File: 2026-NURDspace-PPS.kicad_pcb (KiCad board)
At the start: 4 copper layers, 90 x 85 mm, 122 parts, among them J101 UJ20-C-H-C-4-SMT-TR, Q101 BSN20, Q102 BSN20, Q103 BSN20, Q104 BSN20, Q105 XTR_NFET_SI4134, Q106 XTR_NFET_SI4134, SW101 430172085816, U101 1G126, U102 1G126, U103 1G126, U104 1G126, U105 1G126, U106 1G126, U107 74HC595, U108 1G126, U109 1G126, U110 3.3V, U111 AP33772S, U112 74HC595, U113 1G126, U114 1G126, U115 1G126, U116 1G126, U117 74HC595, U118 1G126, U119 1G126, U120 74HC595, U121 1G126, U122 1G126, U123 481RV12172100, U124 ESP32-S3-WROOM-1

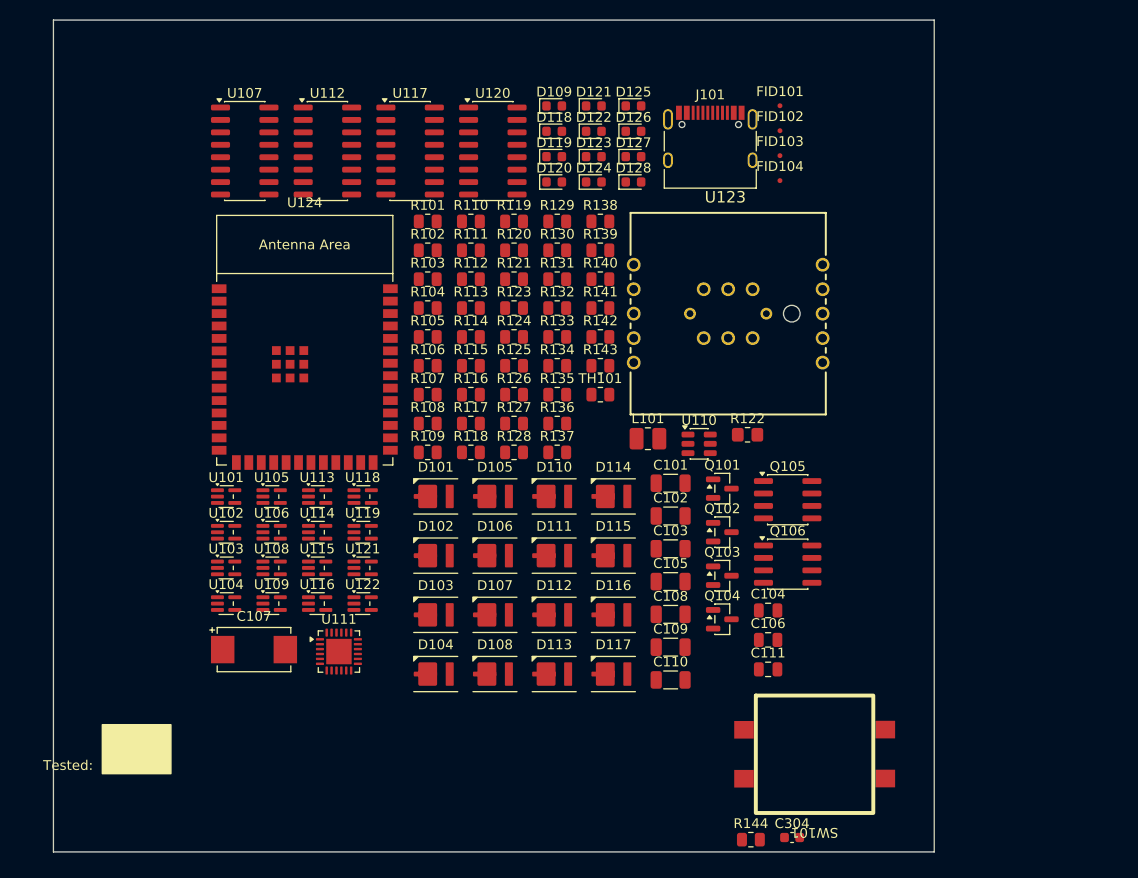
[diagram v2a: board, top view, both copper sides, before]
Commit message: Drawn the schematic
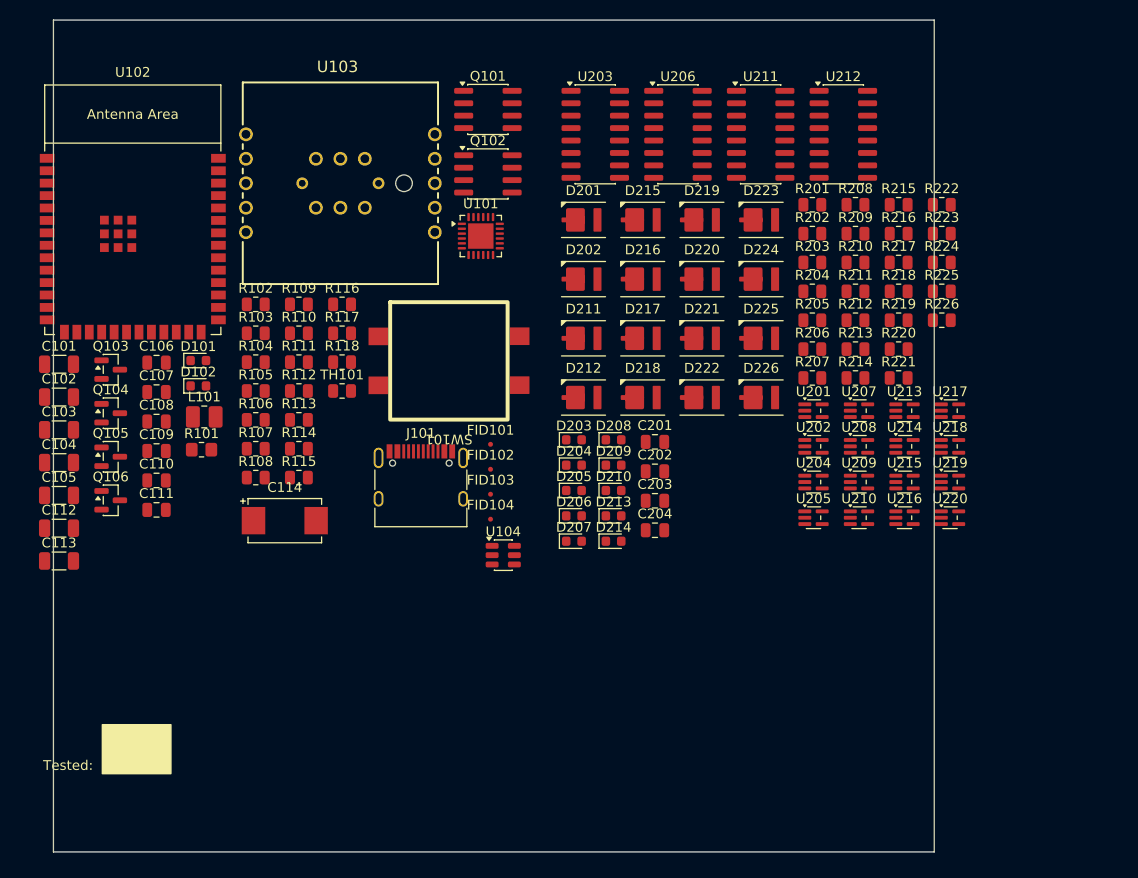
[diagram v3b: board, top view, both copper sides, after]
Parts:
- removed C304: 100nF, Capacitor_SMD:C_0603_1608Metric
- removed D103, D104, D105, D106, D107, D108, D110, D111, D112, D113, D114, D115, D116, D117: MXA8-PW40-0000, 0_NRD_footprints:LED_Luxeon3535_3.5x3.7mm
- removed D109: amber, LED_SMD:LED_0603_1608Metric
- removed D118: brightgreen, LED_SMD:LED_0603_1608Metric
- removed D119, D120, D121, D122, D123, D124, D125, D126, D127, D128: Led_0603_superred_generic, LED_SMD:LED_0603_1608Metric
- removed R119, R120, R123, R124, R125, R126: 39R, Resistor_SMD:R_0805_2012Metric
- removed R121, R127, R128, R130, R131, R137, R138, R144: 5K1, Resistor_SMD:R_0805_2012Metric
- removed R122: 5mR, Resistor_SMD:R_0805_2012Metric_Pad1.20x1.40mm_HandSolder
- removed R129: 180R, Resistor_SMD:R_0805_2012Metric
- removed R132, R133, R134, R135, R136, R139, R140, R141, R142, R143: 270R, Resistor_SMD:R_0805_2012Metric
- removed U105, U106, U108, U109, U113, U114, U115, U116, U118, U119, U121, U122: 1G126, Package_TO_SOT_SMD:SOT-353_SC-70-5
- removed U107, U112, U117, U120: 74HC595, Package_SO:SOIC-16_3.9x9.9mm_P1.27mm
- removed U110: 3.3V, Package_TO_SOT_SMD:TSOT-23-6
- removed U111: AP33772S, Package_DFN_QFN:QFN-24-1EP_4x4mm_P0.5mm_EP2.6x2.6mm
- removed U123: 481RV12172100, 0_NRD_footprints:481RV12172100
- removed U124: ESP32-S3-WROOM-1, 0_NRD_footprints:ESP32-S3-WROOM-1
- added C112: 6.8uF, Capacitor_SMD:C_1206_3216Metric, F.Cu at (103.1, 66.9)
- added C113: 1uF, Capacitor_SMD:C_1206_3216Metric, F.Cu at (103.1, 70.3)
- added C114: 180uF, 0_NRD_footprints:CP_Wurth_WCAP-PHLE-L7.3W4.3H1.9, F.Cu at (126.1, 66.2)
- added C201: 100nF, Capacitor_SMD:C_0805_2012Metric, F.Cu at (164.0, 58.1)
- added C202: 100nF, Capacitor_SMD:C_0805_2012Metric, F.Cu at (164.0, 61.1)
- added C203: 100nF, Capacitor_SMD:C_0805_2012Metric, F.Cu at (164.0, 64.1)
- added C204: 100nF, Capacitor_SMD:C_0805_2012Metric, F.Cu at (164.0, 67.1)
- added D201: MXA8-PW40-0000, 0_NRD_footprints:LED_Luxeon3535_3.5x3.7mm, F.Cu at (156.7, 35.4)
- added D202: MXA8-PW40-0000, 0_NRD_footprints:LED_Luxeon3535_3.5x3.7mm, F.Cu at (156.7, 41.5)
- added D203: Led_0603_superred_generic, LED_SMD:LED_0603_1608Metric, F.Cu at (155.7, 57.9)
- added D204: Led_0603_superred_generic, LED_SMD:LED_0603_1608Metric, F.Cu at (155.7, 60.5)
- added D205: Led_0603_superred_generic, LED_SMD:LED_0603_1608Metric, F.Cu at (155.7, 63.1)
- added D206: Led_0603_superred_generic, LED_SMD:LED_0603_1608Metric, F.Cu at (155.7, 65.7)
- added D207: Led_0603_superred_generic, LED_SMD:LED_0603_1608Metric, F.Cu at (155.7, 68.2)
- added D208: Led_0603_superred_generic, LED_SMD:LED_0603_1608Metric, F.Cu at (159.7, 57.9)
- added D209: Led_0603_superred_generic, LED_SMD:LED_0603_1608Metric, F.Cu at (159.7, 60.5)
- added D210: Led_0603_superred_generic, LED_SMD:LED_0603_1608Metric, F.Cu at (159.7, 63.1)
- added D211: MXA8-PW40-0000, 0_NRD_footprints:LED_Luxeon3535_3.5x3.7mm, F.Cu at (156.7, 47.5)
- added D212: MXA8-PW40-0000, 0_NRD_footprints:LED_Luxeon3535_3.5x3.7mm, F.Cu at (156.7, 53.6)
- added D213: Led_0603_superred_generic, LED_SMD:LED_0603_1608Metric, F.Cu at (159.7, 65.7)
- added D214: Led_0603_superred_generic, LED_SMD:LED_0603_1608Metric, F.Cu at (159.7, 68.2)
- added D215: MXA8-PW40-0000, 0_NRD_footprints:LED_Luxeon3535_3.5x3.7mm, F.Cu at (162.7, 35.4)
- added D216: MXA8-PW40-0000, 0_NRD_footprints:LED_Luxeon3535_3.5x3.7mm, F.Cu at (162.7, 41.5)
- added D217: MXA8-PW40-0000, 0_NRD_footprints:LED_Luxeon3535_3.5x3.7mm, F.Cu at (162.7, 47.5)
- added D218: MXA8-PW40-0000, 0_NRD_footprints:LED_Luxeon3535_3.5x3.7mm, F.Cu at (162.7, 53.6)
- added D219: MXA8-PW40-0000, 0_NRD_footprints:LED_Luxeon3535_3.5x3.7mm, F.Cu at (168.8, 35.4)
- added D220: MXA8-PW40-0000, 0_NRD_footprints:LED_Luxeon3535_3.5x3.7mm, F.Cu at (168.8, 41.5)
- added D221: MXA8-PW40-0000, 0_NRD_footprints:LED_Luxeon3535_3.5x3.7mm, F.Cu at (168.8, 47.5)
- added D222: MXA8-PW40-0000, 0_NRD_footprints:LED_Luxeon3535_3.5x3.7mm, F.Cu at (168.8, 53.6)
- added D223: MXA8-PW40-0000, 0_NRD_footprints:LED_Luxeon3535_3.5x3.7mm, F.Cu at (174.8, 35.4)
- added D224: MXA8-PW40-0000, 0_NRD_footprints:LED_Luxeon3535_3.5x3.7mm, F.Cu at (174.8, 41.5)
- added D225: MXA8-PW40-0000, 0_NRD_footprints:LED_Luxeon3535_3.5x3.7mm, F.Cu at (174.8, 47.5)
- added D226: MXA8-PW40-0000, 0_NRD_footprints:LED_Luxeon3535_3.5x3.7mm, F.Cu at (174.8, 53.6)
- added R201: 39R, Resistor_SMD:R_0805_2012Metric, F.Cu at (180.0, 33.9)
- added R202: 39R, Resistor_SMD:R_0805_2012Metric, F.Cu at (180.0, 36.8)
- added R203: 270R, Resistor_SMD:R_0805_2012Metric, F.Cu at (180.0, 39.8)
- added R204: 270R, Resistor_SMD:R_0805_2012Metric, F.Cu at (180.0, 42.7)
- added R205: 270R, Resistor_SMD:R_0805_2012Metric, F.Cu at (180.0, 45.7)
- added R206: 270R, Resistor_SMD:R_0805_2012Metric, F.Cu at (180.0, 48.6)
- added R207: 270R, Resistor_SMD:R_0805_2012Metric, F.Cu at (180.0, 51.6)
- added R208: 270R, Resistor_SMD:R_0805_2012Metric, F.Cu at (184.5, 33.9)
- added R209: 270R, Resistor_SMD:R_0805_2012Metric, F.Cu at (184.5, 36.8)
- added R210: 270R, Resistor_SMD:R_0805_2012Metric, F.Cu at (184.5, 39.8)
- added R211: 39R, Resistor_SMD:R_0805_2012Metric, F.Cu at (184.5, 42.7)
- added R212: 39R, Resistor_SMD:R_0805_2012Metric, F.Cu at (184.5, 45.7)
- added R213: 270R, Resistor_SMD:R_0805_2012Metric, F.Cu at (184.5, 48.6)
- added R214: 270R, Resistor_SMD:R_0805_2012Metric, F.Cu at (184.5, 51.6)
- added R215: 39R, Resistor_SMD:R_0805_2012Metric, F.Cu at (188.9, 33.9)
- added R216: 39R, Resistor_SMD:R_0805_2012Metric, F.Cu at (188.9, 36.8)
- added R217: 39R, Resistor_SMD:R_0805_2012Metric, F.Cu at (188.9, 39.8)
- added R218: 39R, Resistor_SMD:R_0805_2012Metric, F.Cu at (188.9, 42.7)
- added R219: 39R, Resistor_SMD:R_0805_2012Metric, F.Cu at (188.9, 45.7)
- added R220: 39R, Resistor_SMD:R_0805_2012Metric, F.Cu at (188.9, 48.6)
- added R221: 39R, Resistor_SMD:R_0805_2012Metric, F.Cu at (188.9, 51.6)
- added R222: 39R, Resistor_SMD:R_0805_2012Metric, F.Cu at (193.3, 33.9)
- added R223: 39R, Resistor_SMD:R_0805_2012Metric, F.Cu at (193.3, 36.8)
- added R224: 39R, Resistor_SMD:R_0805_2012Metric, F.Cu at (193.3, 39.8)
- added R225: 39R, Resistor_SMD:R_0805_2012Metric, F.Cu at (193.3, 42.7)
- added R226: 39R, Resistor_SMD:R_0805_2012Metric, F.Cu at (193.3, 45.7)
- added U201: 1G126, Package_TO_SOT_SMD:SOT-353_SC-70-5, F.Cu at (180.2, 54.9)
- added U202: 1G126, Package_TO_SOT_SMD:SOT-353_SC-70-5, F.Cu at (180.2, 58.6)
- added U203: 74HC595, Package_SO:SOIC-16_3.9x9.9mm_P1.27mm, F.Cu at (157.9, 26.7)
- added U204: 1G126, Package_TO_SOT_SMD:SOT-353_SC-70-5, F.Cu at (180.2, 62.2)
- added U205: 1G126, Package_TO_SOT_SMD:SOT-353_SC-70-5, F.Cu at (180.2, 65.8)
- added U206: 74HC595, Package_SO:SOIC-16_3.9x9.9mm_P1.27mm, F.Cu at (166.3, 26.7)
- added U207: 1G126, Package_TO_SOT_SMD:SOT-353_SC-70-5, F.Cu at (184.8, 54.9)
- added U208: 1G126, Package_TO_SOT_SMD:SOT-353_SC-70-5, F.Cu at (184.8, 58.6)
- added U209: 1G126, Package_TO_SOT_SMD:SOT-353_SC-70-5, F.Cu at (184.8, 62.2)
- added U210: 1G126, Package_TO_SOT_SMD:SOT-353_SC-70-5, F.Cu at (184.8, 65.8)
- added U211: 74HC595, Package_SO:SOIC-16_3.9x9.9mm_P1.27mm, F.Cu at (174.8, 26.7)
- added U212: 74HC595, Package_SO:SOIC-16_3.9x9.9mm_P1.27mm, F.Cu at (183.2, 26.7)
- added U213: 1G126, Package_TO_SOT_SMD:SOT-353_SC-70-5, F.Cu at (189.5, 54.9)
- added U214: 1G126, Package_TO_SOT_SMD:SOT-353_SC-70-5, F.Cu at (189.5, 58.6)
- added U215: 1G126, Package_TO_SOT_SMD:SOT-353_SC-70-5, F.Cu at (189.5, 62.2)
- added U216: 1G126, Package_TO_SOT_SMD:SOT-353_SC-70-5, F.Cu at (189.5, 65.8)
- added U217: 1G126, Package_TO_SOT_SMD:SOT-353_SC-70-5, F.Cu at (194.1, 54.9)
- added U218: 1G126, Package_TO_SOT_SMD:SOT-353_SC-70-5, F.Cu at (194.1, 58.6)
- added U219: 1G126, Package_TO_SOT_SMD:SOT-353_SC-70-5, F.Cu at (194.1, 62.2)
- added U220: 1G126, Package_TO_SOT_SMD:SOT-353_SC-70-5, F.Cu at (194.1, 65.8)
- C104: value 100nF -> 6.8uF; footprint Capacitor_SMD:C_0805_2012Metric -> Capacitor_SMD:C_1206_3216Metric
- C107: value 180uF -> 100nF; footprint 0_NRD_footprints:CP_Wurth_WCAP-PHLE-L7.3W4.3H1.9 -> Capacitor_SMD:C_0805_2012Metric
- C108, C110: value 6.8uF -> 100nF; footprint Capacitor_SMD:C_1206_3216Metric -> Capacitor_SMD:C_0805_2012Metric
- C109: value 1uF -> 100nF; footprint Capacitor_SMD:C_1206_3216Metric -> Capacitor_SMD:C_0805_2012Metric
- D101: value MXA8-PW40-0000 -> brightgreen; footprint 0_NRD_footprints:LED_Luxeon3535_3.5x3.7mm -> LED_SMD:LED_0603_1608Metric
- D102: value MXA8-PW40-0000 -> amber; footprint 0_NRD_footprints:LED_Luxeon3535_3.5x3.7mm -> LED_SMD:LED_0603_1608Metric
- Q101, Q102: value BSN20 -> XTR_NFET_SI4134; footprint Package_TO_SOT_SMD:SOT-23 -> Package_SO:SOIC-8_3.9x4.9mm_P1.27mm
- Q105, Q106: value XTR_NFET_SI4134 -> BSN20; footprint Package_SO:SOIC-8_3.9x4.9mm_P1.27mm -> Package_TO_SOT_SMD:SOT-23
- R101: value 5K1 -> 5mR; footprint Resistor_SMD:R_0805_2012Metric -> Resistor_SMD:R_0805_2012Metric_Pad1.20x1.40mm_HandSolder
- R105: value 39R -> 180R
- R106, R107, R108, R109, R110, R111, R112, R117, R118: value 39R -> 5K1
- U101: value 1G126 -> AP33772S; footprint Package_TO_SOT_SMD:SOT-353_SC-70-5 -> Package_DFN_QFN:QFN-24-1EP_4x4mm_P0.5mm_EP2.6x2.6mm
- U102: value 1G126 -> ESP32-S3-WROOM-1; footprint Package_TO_SOT_SMD:SOT-353_SC-70-5 -> 0_NRD_footprints:ESP32-S3-WROOM-1
- U103: value 1G126 -> 481RV12172100; footprint Package_TO_SOT_SMD:SOT-353_SC-70-5 -> 0_NRD_footprints:481RV12172100
- U104: value 1G126 -> 3.3V; footprint Package_TO_SOT_SMD:SOT-353_SC-70-5 -> Package_TO_SOT_SMD:TSOT-23-6
- moved C104 74.0 mm to (103.1, 60.2)
- moved Q106 69.5 mm to (108.4, 64.1)
- moved Q105 69.3 mm to (108.4, 59.6)
- moved C106 68.6 mm to (113.0, 50.0)
- moved Q103 65.9 mm to (108.4, 50.7)
- moved Q104 65.9 mm to (108.4, 55.2)
- moved C111 64.6 mm to (113.0, 65.0)
- moved C101 63.7 mm to (103.1, 50.2)
- moved C102 63.7 mm to (103.1, 53.5)
- moved C103 63.7 mm to (103.1, 56.9)
- moved C105 63.1 mm to (103.1, 63.6)
- moved C110 56.3 mm to (113.0, 62.0)
- moved C109 56.2 mm to (113.0, 59.0)
- moved C108 56.1 mm to (113.0, 56.0)
- moved SW101 54.9 mm to (142.9, 49.8)
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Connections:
- C101 pad 1: unconnected-(C101-Pad1) -> Net-(U101-VCC)
- C101 pad 2: unconnected-(C101-Pad2) -> GND
- C102 pad 1: unconnected-(C102-Pad1) -> Net-(U101-VCC)
- C102 pad 2: unconnected-(C102-Pad2) -> GND
- C103 pad 1: unconnected-(C103-Pad1) -> VBUS
- C103 pad 2: unconnected-(C103-Pad2) -> GND
- C104 pad 1: unconnected-(C104-Pad1) -> VBUS
- C104 pad 2: unconnected-(C104-Pad2) -> GND
- C105 pad 1: unconnected-(C105-Pad1) -> +5V
- C105 pad 2: unconnected-(C105-Pad2) -> GND
- C106 pad 1: unconnected-(C106-Pad1) -> Net-(U101-V18)
- C106 pad 2: unconnected-(C106-Pad2) -> GND
- C107 pad 1: unconnected-(C107-Pad1) -> ESP_BOOTSEL
- C107 pad 2: unconnected-(C107-Pad2) -> GND
- C108 pad 1: unconnected-(C108-Pad1) -> +3.3V
- C108 pad 2: unconnected-(C108-Pad2) -> GND
- C109 pad 1: unconnected-(C109-Pad1) -> Net-(U101-IFB)
- C109 pad 2: unconnected-(C109-Pad2) -> GND
- C110 pad 1: unconnected-(C110-Pad1) -> Net-(U102-EN)
- C110 pad 2: unconnected-(C110-Pad2) -> GND
- C111 pad 1: unconnected-(C111-Pad1) -> Net-(U104-BST)
- C111 pad 2: unconnected-(C111-Pad2) -> Net-(U104-SW)
- D101 pad 1: unconnected-(D101-K-Pad1) -> GND
- D101 pad 2: unconnected-(D101-A-Pad2) -> Net-(D101-A)
- D102 pad 1: unconnected-(D102-K-Pad1) -> GND
- D102 pad 2: unconnected-(D102-A-Pad2) -> Net-(D102-A)
- J101 pad A1: Net-(J101-GND-PadA1) -> GND
- J101 pad A12: Net-(J101-GND-PadA1) -> GND
- J101 pad A4: Net-(J101-VBUS-PadA4) -> Net-(U101-ISENP)
- J101 pad A5: unconnected-(J101-CC1-PadA5) -> Net-(J101-CC1)
- J101 pad A6: unconnected-(J101-D+-PadA6) -> D+
- J101 pad A7: unconnected-(J101-D--PadA7) -> D-
- J101 pad A9: Net-(J101-VBUS-PadA4) -> Net-(U101-ISENP)
- J101 pad B1: Net-(J101-GND-PadA1) -> GND
- J101 pad B12: Net-(J101-GND-PadA1) -> GND
- J101 pad B4: Net-(J101-VBUS-PadA4) -> Net-(U101-ISENP)
- J101 pad B5: unconnected-(J101-CC2-PadB5) -> Net-(J101-CC2)
- J101 pad B6: unconnected-(J101-D+-PadB6) -> D+
- J101 pad B7: unconnected-(J101-D--PadB7) -> D-
- J101 pad B9: Net-(J101-VBUS-PadA4) -> Net-(U101-ISENP)
- J101 pad S1: unconnected-(J101-SHIELD-PadS1) -> GND
- L101 pad 1: unconnected-(L101-Pad1) -> Net-(U104-SW)
- L101 pad 2: unconnected-(L101-Pad2) -> +3.3V
- Q101 pad 1: unconnected-(Q101-G-Pad1) -> Net-(Q101-S-Pad1)
- Q101 pad 2: unconnected-(Q101-S-Pad2) -> Net-(Q101-S-Pad1)
- Q101 pad 3: unconnected-(Q101-D-Pad3) -> Net-(Q101-S-Pad1)
- Q102 pad 1: unconnected-(Q102-G-Pad1) -> Net-(Q101-S-Pad1)
- Q102 pad 2: unconnected-(Q102-S-Pad2) -> Net-(Q101-S-Pad1)
- Q102 pad 3: unconnected-(Q102-D-Pad3) -> Net-(Q101-S-Pad1)
- Q103 pad 1: unconnected-(Q103-G-Pad1) -> +5V
- Q103 pad 2: unconnected-(Q103-S-Pad2) -> I^{2}C_{SDA5V}
- Q103 pad 3: unconnected-(Q103-D-Pad3) -> Net-(Q103-D)
- Q104 pad 1: unconnected-(Q104-G-Pad1) -> +3.3V
- Q104 pad 2: unconnected-(Q104-S-Pad2) -> I^{2}C_{SDA3V3}
- Q104 pad 3: unconnected-(Q104-D-Pad3) -> Net-(Q103-D)
- Q105 pad 1: Net-(Q105-S-Pad1) -> +5V
- Q105 pad 2: Net-(Q105-S-Pad1) -> I^{2}C_{SCL5V}
- Q105 pad 3: Net-(Q105-S-Pad1) -> Net-(Q105-D)
- Q106 pad 1: Net-(Q106-S-Pad1) -> +3.3V
- Q106 pad 2: Net-(Q106-S-Pad1) -> Net-(Q105-D)
- Q106 pad 3: Net-(Q106-S-Pad1) -> I^{2}C_{SCL3V3}
- R101 pad 1: unconnected-(R101-Pad1) -> Net-(U101-ISENP)
- R101 pad 2: unconnected-(R101-Pad2) -> Net-(U101-VCC)
- R102 pad 1: unconnected-(R102-Pad1) -> VBUS
- R102 pad 2: unconnected-(R102-Pad2) -> Net-(R102-Pad2)
- R103 pad 1: unconnected-(R103-Pad1) -> Net-(R102-Pad2)
- R103 pad 2: unconnected-(R103-Pad2) -> Net-(D101-A)
- R104 pad 1: unconnected-(R104-Pad1) -> Net-(Q101-G)
- R104 pad 2: unconnected-(R104-Pad2) -> Net-(U101-PWR_EN)
- R105 pad 1: unconnected-(R105-Pad1) -> VBUS
- R105 pad 2: unconnected-(R105-Pad2) -> Net-(U101-VOUT)
- R106 pad 1: unconnected-(R106-Pad1) -> Net-(J101-CC2)
- R106 pad 2: unconnected-(R106-Pad2) -> GND
- R107 pad 1: unconnected-(R107-Pad1) -> Net-(J101-CC1)
- R107 pad 2: unconnected-(R107-Pad2) -> GND
- R108 pad 1: unconnected-(R108-Pad1) -> +3.3V
- R108 pad 2: unconnected-(R108-Pad2) -> ESP_BOOTSEL
- R109 pad 1: unconnected-(R109-Pad1) -> +3.3V
- R109 pad 2: unconnected-(R109-Pad2) -> Net-(U102-EN)
- R110 pad 1: unconnected-(R110-Pad1) -> +3.3V
- R110 pad 2: unconnected-(R110-Pad2) -> ~{CLR}
- R111 pad 1: unconnected-(R111-Pad1) -> Net-(U101-LED)
- R111 pad 2: unconnected-(R111-Pad2) -> Net-(D102-A)
- R112 pad 1: unconnected-(R112-Pad1) -> OE
- R112 pad 2: unconnected-(R112-Pad2) -> GND
- R113 pad 1: unconnected-(R113-Pad1) -> +5V
- R113 pad 2: unconnected-(R113-Pad2) -> I^{2}C_{SDA5V}
- R114 pad 1: unconnected-(R114-Pad1) -> +3.3V
- R114 pad 2: unconnected-(R114-Pad2) -> I^{2}C_{SDA3V3}
- R115 pad 1: unconnected-(R115-Pad1) -> +3.3V
- R115 pad 2: unconnected-(R115-Pad2) -> Net-(R115-Pad2)
- R116 pad 1: unconnected-(R116-Pad1) -> +5V
- R116 pad 2: unconnected-(R116-Pad2) -> I^{2}C_{SCL5V}
- R117 pad 1: unconnected-(R117-Pad1) -> +3.3V
- R117 pad 2: unconnected-(R117-Pad2) -> I^{2}C_{SCL3V3}
- R118 pad 1: unconnected-(R118-Pad1) -> +3.3V
- R118 pad 2: unconnected-(R118-Pad2) -> Net-(U102-GPIO21)
- TH101 pad 1: unconnected-(TH101-Pad1) -> Net-(U101-OTP)
- TH101 pad 2: unconnected-(TH101-Pad2) -> GND
- U101 pad 1: unconnected-(U101-OE-Pad1) -> Net-(U101-ISENP)
- U101 pad 2: unconnected-(U101-A-Pad2) -> Net-(U101-NC-Pad10)
- U101 pad 3: unconnected-(U101-GND-Pad3) -> GND
- U101 pad 4: unconnected-(U101-Y-Pad4) -> I^{2}C_{SDA5V}
- U101 pad 5: unconnected-(U101-VCC-Pad5) -> I^{2}C_{SCL5V}
- U102 pad 1: unconnected-(U102-OE-Pad1) -> GND
- U102 pad 2: unconnected-(U102-A-Pad2) -> +3.3V
- U102 pad 3: unconnected-(U102-GND-Pad3) -> Net-(U102-EN)
- U102 pad 4: unconnected-(U102-Y-Pad4) -> Net-(U102-GPIO4/TOUCH4/ADC1_CH3)
- U102 pad 5: unconnected-(U102-VCC-Pad5) -> Net-(U102-GPIO5/TOUCH5/ADC1_CH4)
- U103 pad 1: unconnected-(U103-OE-Pad1) -> Net-(U102-GPIO3/TOUCH3/ADC1_CH2)
- U103 pad 2: unconnected-(U103-A-Pad2) -> Net-(U102-GPIO4/TOUCH4/ADC1_CH3)
- U103 pad 3: unconnected-(U103-GND-Pad3) -> Net-(U102-GPIO5/TOUCH5/ADC1_CH4)
- U103 pad 4: unconnected-(U103-Y-Pad4) -> Net-(U102-GPIO6/TOUCH6/ADC1_CH5)
- U103 pad 5: unconnected-(U103-VCC-Pad5) -> Net-(U102-GPIO9/TOUCH9/ADC1_CH8/FSPIHD/SUBSPIHD)
- U104 pad 1: unconnected-(U104-OE-Pad1) -> +3.3V
- U104 pad 2: unconnected-(U104-A-Pad2) -> VBUS
- U104 pad 3: unconnected-(U104-GND-Pad3) -> VBUS
- U104 pad 4: unconnected-(U104-Y-Pad4) -> GND
- U104 pad 5: unconnected-(U104-VCC-Pad5) -> Net-(U104-SW)

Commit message: First version of layout
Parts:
- added C115: 100nF, Capacitor_SMD:C_0805_2012Metric, F.Cu at (137.0, 80.0)
- added D227: Led_0603_superred_generic, LED_SMD:LED_0603_1608Metric, F.Cu at (148.0, 70.1)
- added D228: Led_0603_superred_generic, LED_SMD:LED_0603_1608Metric, F.Cu at (148.0, 72.7)
- added J201: BM05B, 0_NRD_footprints:J_BM05B-GHS-TBT, F.Cu at (165.5, 65.0)
- added R227: 270R, Resistor_SMD:R_0805_2012Metric, F.Cu at (160.0, 69.5)
- added R228: 270R, Resistor_SMD:R_0805_2012Metric, F.Cu at (160.0, 71.5)
- added U221: 1G126, Package_TO_SOT_SMD:SOT-353_SC-70-5, F.Cu at (112.0, 97.5)
- added U222: 74HC595, Package_SO:SOIC-16_3.9x9.9mm_P1.27mm, F.Cu at (155.0, 50.0)
- C104, C112: value 6.8uF -> 100nF; footprint Capacitor_SMD:C_1206_3216Metric -> Capacitor_SMD:C_0805_2012Metric
- C106: value 100nF -> 1uF; footprint Capacitor_SMD:C_0805_2012Metric -> Capacitor_SMD:C_1206_3216Metric
- C108, C111: value 100nF -> 6.8uF; footprint Capacitor_SMD:C_0805_2012Metric -> Capacitor_SMD:C_1206_3216Metric
- C110: value 100nF -> 180uF; footprint Capacitor_SMD:C_0805_2012Metric -> 0_NRD_footprints:CP_Wurth_WCAP-PHLE-L7.3W4.3H1.9
- C113: value 1uF -> 100nF; footprint Capacitor_SMD:C_1206_3216Metric -> Capacitor_SMD:C_0805_2012Metric
- C114: value 180uF -> 100nF; footprint 0_NRD_footprints:CP_Wurth_WCAP-PHLE-L7.3W4.3H1.9 -> Capacitor_SMD:C_0805_2012Metric
- D101: value brightgreen -> amber
- D102: value amber -> brightgreen
- D203, D204, D205, D206, D207, D208, D209, D210, D213, D214: value Led_0603_superred_generic -> MXA8-PW40-0000; footprint LED_SMD:LED_0603_1608Metric -> 0_NRD_footprints:LED_Luxeon3535_3.5x3.7mm
- D219, D220, D221, D222, D223, D224, D225, D226: value MXA8-PW40-0000 -> Led_0603_superred_generic; footprint 0_NRD_footprints:LED_Luxeon3535_3.5x3.7mm -> LED_SMD:LED_0603_1608Metric
- Q101, Q102: value XTR_NFET_SI4134 -> BSN20; footprint Package_SO:SOIC-8_3.9x4.9mm_P1.27mm -> Package_TO_SOT_SMD:SOT-23
- Q105, Q106: value BSN20 -> XTR_NFET_SI4134; footprint Package_TO_SOT_SMD:SOT-23 -> Package_SO:SOIC-8_3.9x4.9mm_P1.27mm
- R101: value 5mR -> 5K1; footprint Resistor_SMD:R_0805_2012Metric_Pad1.20x1.40mm_HandSolder -> Resistor_SMD:R_0805_2012Metric
- R105: value 180R -> 5K1
- R107: value 5K1 -> 5mR; footprint Resistor_SMD:R_0805_2012Metric -> Resistor_SMD:R_0805_2012Metric_Pad1.20x1.40mm_HandSolder
- R110: value 5K1 -> 180R
- R203, R204, R205, R206, R207, R208, R209, R210, R213, R214: value 270R -> 39R
- R219, R220, R221, R222, R223, R224, R225, R226: value 39R -> 270R
- SW101: value 430172085816 -> 430483025816; footprint 0_NRD_footprints:btn_momentary_430172085816 -> 0_NRD_footprints:SW_Push_430483025816
- U101: value AP33772S -> 3.3V; footprint Package_DFN_QFN:QFN-24-1EP_4x4mm_P0.5mm_EP2.6x2.6mm -> Package_TO_SOT_SMD:TSOT-23-6
- U102: value ESP32-S3-WROOM-1 -> AP33772S; footprint 0_NRD_footprints:ESP32-S3-WROOM-1 -> Package_DFN_QFN:QFN-24-1EP_4x4mm_P0.5mm_EP2.6x2.6mm
- U103: value 481RV12172100 -> ESP32-S3-WROOM-1; footprint 0_NRD_footprints:481RV12172100 -> 0_NRD_footprints:ESP32-S3-WROOM-1
- U104: value 3.3V -> 481RV12172100; footprint Package_TO_SOT_SMD:TSOT-23-6 -> 0_NRD_footprints:481RV12172100
- U201, U210, U219: value 1G126 -> 74HC595; footprint Package_TO_SOT_SMD:SOT-353_SC-70-5 -> Package_SO:SOIC-16_3.9x9.9mm_P1.27mm
- U203, U206, U211, U212: value 74HC595 -> 1G126; footprint Package_SO:SOIC-16_3.9x9.9mm_P1.27mm -> Package_TO_SOT_SMD:SOT-353_SC-70-5
- moved R218 92.1 mm to (112.0, 93.5), turned to 90 degrees
- moved R217 91.5 mm to (114.8, 93.5), turned to 90 degrees
- moved R216 91.2 mm to (117.5, 93.5), turned to 90 degrees
- moved R215 91.0 mm to (120.2, 93.5), turned to 90 degrees
- moved R222 90.6 mm to (110.0, 69.5)
- moved R223 90.2 mm to (110.0, 71.5)
- moved U212 86.4 mm to (133.7, 97.5), turned to 90 degrees
- moved U218 86.0 mm to (117.5, 97.5), turned to 90 degrees
- moved U220 85.4 mm to (114.8, 97.5), turned to 90 degrees
- moved U217 85.3 mm to (120.2, 97.5), turned to 90 degrees
- moved R219 80.9 mm to (110.0, 63.5)
- moved R220 80.6 mm to (110.0, 65.5)
- moved U211 80.6 mm to (136.3, 97.5), turned to 90 degrees
- moved R221 80.5 mm to (110.0, 67.5)
- moved U219 80.0 mm to (115.0, 50.0), turned to -45 degrees
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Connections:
- C101 pad 1: Net-(U101-VCC) -> Net-(U102-VCC)
- C102 pad 1: Net-(U101-VCC) -> Net-(U102-VCC)
- C104 pad 1: VBUS -> Net-(U101-BST)
- C104 pad 2: GND -> Net-(U101-SW)
- C106 pad 1: Net-(U101-V18) -> +3.3V
- C107 pad 1: ESP_BOOTSEL -> Net-(U102-V18)
- C108 pad 1: +3.3V -> VBUS
- C109 pad 1: Net-(U101-IFB) -> Net-(U102-IFB)
- C110 pad 1: Net-(U102-EN) -> +3.3V
- C111 pad 1: Net-(U104-BST) -> VBUS
- C111 pad 2: Net-(U104-SW) -> GND
- C112 pad 1: VBUS -> Net-(U103-EN)
- C114 pad 1: +3.3V -> ESP_BOOTSEL
- J101 pad A4: Net-(U101-ISENP) -> Net-(U102-ISENP)
- J101 pad A9: Net-(U101-ISENP) -> Net-(U102-ISENP)
- J101 pad B4: Net-(U101-ISENP) -> Net-(U102-ISENP)
- J101 pad B9: Net-(U101-ISENP) -> Net-(U102-ISENP)
- L101 pad 1: Net-(U104-SW) -> Net-(U101-SW)
- Q101 pad 1: Net-(Q101-S-Pad1) -> +5V
- Q101 pad 2: Net-(Q101-S-Pad1) -> I^{2}C_{SDA5V}
- Q101 pad 3: Net-(Q101-S-Pad1) -> Net-(Q101-D)
- Q102 pad 1: Net-(Q101-S-Pad1) -> +5V
- Q102 pad 2: Net-(Q101-S-Pad1) -> I^{2}C_{SCL5V}
- Q102 pad 3: Net-(Q101-S-Pad1) -> Net-(Q102-D)
- Q103 pad 1: +5V -> +3.3V
- Q103 pad 2: I^{2}C_{SDA5V} -> I^{2}C_{SDA3V3}
- Q103 pad 3: Net-(Q103-D) -> Net-(Q101-D)
- Q104 pad 2: I^{2}C_{SDA3V3} -> I^{2}C_{SCL3V3}
- Q104 pad 3: Net-(Q103-D) -> Net-(Q102-D)
- Q105 pad 1: +5V -> Net-(Q105-S-Pad1)
- Q105 pad 2: I^{2}C_{SCL5V} -> Net-(Q105-S-Pad1)
- Q105 pad 3: Net-(Q105-D) -> Net-(Q105-S-Pad1)
- Q106 pad 1: +3.3V -> Net-(Q105-S-Pad1)
- Q106 pad 2: Net-(Q105-D) -> Net-(Q105-S-Pad1)
- Q106 pad 3: I^{2}C_{SCL3V3} -> Net-(Q105-S-Pad1)
- R101 pad 1: Net-(U101-ISENP) -> +5V
- R101 pad 2: Net-(U101-VCC) -> I^{2}C_{SDA5V}
- R102 pad 1: VBUS -> +5V
- R102 pad 2: Net-(R102-Pad2) -> I^{2}C_{SCL5V}
- R103 pad 1: Net-(R102-Pad2) -> Net-(J101-CC2)
- R103 pad 2: Net-(D101-A) -> GND
- R104 pad 1: Net-(Q101-G) -> Net-(J101-CC1)
- R104 pad 2: Net-(U101-PWR_EN) -> GND
- R105 pad 1: VBUS -> +3.3V
- R105 pad 2: Net-(U101-VOUT) -> I^{2}C_{SDA3V3}
- R106 pad 1: Net-(J101-CC2) -> +3.3V
- R106 pad 2: GND -> I^{2}C_{SCL3V3}
- R107 pad 1: Net-(J101-CC1) -> Net-(U102-ISENP)
- R107 pad 2: GND -> Net-(U102-VCC)
- R108 pad 1: +3.3V -> Net-(Q105-G)
- R108 pad 2: ESP_BOOTSEL -> Net-(U102-PWR_EN)
- R109 pad 1: +3.3V -> Net-(U102-LED)
- R109 pad 2: Net-(U102-EN) -> Net-(D101-A)
- R110 pad 1: +3.3V -> VBUS
- R110 pad 2: ~{CLR} -> Net-(U102-VOUT)
- R111 pad 1: Net-(U101-LED) -> VBUS
- R111 pad 2: Net-(D102-A) -> Net-(R111-Pad2)
- R112 pad 1: OE -> Net-(R111-Pad2)
- R112 pad 2: GND -> Net-(D102-A)
- R113 pad 1: +5V -> +3.3V
- R113 pad 2: I^{2}C_{SDA5V} -> Net-(U103-EN)
- R114 pad 2: I^{2}C_{SDA3V3} -> ESP_BOOTSEL
- R115 pad 2: Net-(R115-Pad2) -> Net-(U103-GPIO21)
- R116 pad 1: +5V -> +3.3V
- R116 pad 2: I^{2}C_{SCL5V} -> ~{CLR}
- R117 pad 1: +3.3V -> OE
- R117 pad 2: I^{2}C_{SCL3V3} -> GND
- R118 pad 2: Net-(U102-GPIO21) -> Net-(C115-Pad1)
- R201 pad 1: Net-(U201-Y) -> Net-(U202-Y)
- R202 pad 1: Net-(U202-Y) -> Net-(U203-Y)
- R203 pad 1: Net-(U203-QA) -> Net-(U204-Y)
- R204 pad 1: Net-(U203-QB) -> Net-(U205-Y)
- R205 pad 1: Net-(U203-QC) -> Net-(U206-Y)
- R206 pad 1: Net-(U203-QD) -> Net-(U207-Y)
- R207 pad 1: Net-(U203-QE) -> Net-(U208-Y)
- R208 pad 1: Net-(U203-QF) -> Net-(U209-Y)
- R209 pad 1: Net-(U203-QG) -> Net-(U211-Y)
- R210 pad 1: Net-(U203-QH) -> Net-(U212-Y)
- R211 pad 1: Net-(U204-Y) -> Net-(U213-Y)
- R212 pad 1: Net-(U205-Y) -> Net-(U214-Y)
- R213 pad 1: Net-(U206-QA) -> Net-(U215-Y)
- R214 pad 1: Net-(U206-QB) -> Net-(U216-Y)
- R215 pad 1: Net-(U207-Y) -> Net-(U217-Y)
- R216 pad 1: Net-(U208-Y) -> Net-(U218-Y)
- R217 pad 1: Net-(U209-Y) -> Net-(U220-Y)
- R218 pad 1: Net-(U210-Y) -> Net-(U221-Y)
- R219 pad 1: Net-(U213-Y) -> Net-(U219-QC)
- R220 pad 1: Net-(U214-Y) -> Net-(U219-QD)
- R221 pad 1: Net-(U215-Y) -> Net-(U219-QE)
- R222 pad 1: Net-(U216-Y) -> Net-(U219-QF)
- R223 pad 1: Net-(U217-Y) -> Net-(U219-QG)
- R224 pad 1: Net-(U218-Y) -> Net-(U219-QH)
- R225 pad 1: Net-(U219-Y) -> Net-(U222-QA)
- R226 pad 1: Net-(U220-Y) -> Net-(U222-QB)
- TH101 pad 1: Net-(U101-OTP) -> Net-(U102-OTP)
- U101 pad 1: Net-(U101-ISENP) -> +3.3V
- U101 pad 2: Net-(U101-NC-Pad10) -> VBUS
- U101 pad 3: GND -> VBUS
- U101 pad 4: I^{2}C_{SDA5V} -> GND
- U101 pad 5: I^{2}C_{SCL5V} -> Net-(U101-SW)
- U101 pad 6: unconnected-(U101-FLIP-Pad6) -> Net-(U101-BST)
- U102 pad 1: GND -> Net-(U102-ISENP)
- U102 pad 11: DATA1 -> unconnected-(U102-NC-Pad11)
- U102 pad 12: CLK -> Net-(U102-V18)
- U102 pad 13: D- -> Net-(U102-OTP)
- U102 pad 14: D+ -> unconnected-(U102-NC-Pad14)
- U102 pad 15: Net-(U102-GPIO3/TOUCH3/ADC1_CH2) -> Net-(U102-IFB)
- U102 pad 16: unconnected-(U102-GPIO46-Pad16) -> Net-(J101-CC2)
- U102 pad 17: Net-(U102-GPIO9/TOUCH9/ADC1_CH8/FSPIHD/SUBSPIHD) -> Net-(J101-CC1)
- U102 pad 18: Net-(U102-GPIO10/TOUCH10/ADC1_CH9/FSPICS0/FSPIIO4/SUBSPICS0) -> unconnected-(U102-DN-Pad18)
- U102 pad 19: Net-(U102-GPIO11/TOUCH11/ADC2_CH0/FSPID/FSPIIO5/SUBSPID) -> unconnected-(U102-DP-Pad19)
- U102 pad 2: +3.3V -> unconnected-(U102-NC-Pad2)
- U102 pad 20: Net-(U102-GPIO12/TOUCH12/ADC2_CH1/FSPICLK/FSPIIO6/SUBSPICLK) -> +5V
- U102 pad 21: Net-(U102-GPIO13/TOUCH13/ADC2_CH2/FSPIQ/FSPIIO7/SUBSPIQ) -> unconnected-(U102-NC-Pad21)
- U102 pad 22: Net-(U102-GPIO14/TOUCH14/ADC2_CH3/FSPIWP/FSPIDQS/SUBSPIWP) -> Net-(U102-VOUT)
- U102 pad 23: Net-(U102-GPIO21) -> Net-(U102-PWR_EN)
- U102 pad 24: unconnected-(U102-GPIO47/SPICLK_P/SUBSPICLK_P_DIFF-Pad24) -> Net-(U102-VCC)
- U102 pad 25: unconnected-(U102-GPIO48/SPICLK_N/SUBSPICLK_N_DIFF-Pad25) -> GND
- U102 pad 3: Net-(U102-EN) -> GND
- U102 pad 4: Net-(U102-GPIO4/TOUCH4/ADC1_CH3) -> I^{2}C_{SDA5V}
- U102 pad 5: Net-(U102-GPIO5/TOUCH5/ADC1_CH4) -> I^{2}C_{SCL5V}
- U102 pad 6: Net-(U102-GPIO6/TOUCH6/ADC1_CH5) -> unconnected-(U102-FLIP-Pad6)
- U102 pad 8: unconnected-(U102-GPIO15/U0RTS/ADC2_CH4/XTAL_32K_P-Pad8) -> Net-(U102-LED)
- U103 pad 1: Net-(U102-GPIO3/TOUCH3/ADC1_CH2) -> GND
- U103 pad 11: unconnected-(U103-Pad11) -> DATA1
- U103 pad 12: Net-(U102-GPIO21) -> CLK
- U103 pad 13: GND -> D-
- U103 pad 14: unconnected-(U103-Pad14) -> D+
- U103 pad 15: unconnected-(U103-Pad15) -> Net-(U103-GPIO3/TOUCH3/ADC1_CH2)
- U103 pad 2: Net-(U102-GPIO4/TOUCH4/ADC1_CH3) -> +3.3V
- U103 pad 3: Net-(U102-GPIO5/TOUCH5/ADC1_CH4) -> Net-(U103-EN)
- U103 pad 4: Net-(U102-GPIO6/TOUCH6/ADC1_CH5) -> Net-(U103-GPIO4/TOUCH4/ADC1_CH3)
- U103 pad 5: Net-(U102-GPIO9/TOUCH9/ADC1_CH8/FSPIHD/SUBSPIHD) -> Net-(U103-GPIO5/TOUCH5/ADC1_CH4)
- U103 pad 6: Net-(U102-GPIO10/TOUCH10/ADC1_CH9/FSPICS0/FSPIIO4/SUBSPICS0) -> Net-(U103-GPIO6/TOUCH6/ADC1_CH5)
- U103 pad 7: Net-(U102-GPIO11/TOUCH11/ADC2_CH0/FSPID/FSPIIO5/SUBSPID) -> unconnected-(U103-GPIO7/TOUCH7/ADC1_CH6-Pad7)
- U103 pad 8: Net-(U102-GPIO12/TOUCH12/ADC2_CH1/FSPICLK/FSPIIO6/SUBSPICLK) -> I^{2}C_{SCL3V3}
- U104 pad 1: +3.3V -> Net-(U103-GPIO3/TOUCH3/ADC1_CH2)
- U104 pad 2: VBUS -> Net-(U103-GPIO4/TOUCH4/ADC1_CH3)
- U104 pad 3: VBUS -> Net-(U103-GPIO5/TOUCH5/ADC1_CH4)
- U104 pad 4: GND -> Net-(U103-GPIO6/TOUCH6/ADC1_CH5)
- U104 pad 5: Net-(U104-SW) -> Net-(U103-GPIO9/TOUCH9/ADC1_CH8/FSPIHD/SUBSPIHD)
- U104 pad 6: Net-(U104-BST) -> Net-(U103-GPIO10/TOUCH10/ADC1_CH9/FSPICS0/FSPIIO4/SUBSPICS0)
- U201 pad 1: OE -> Net-(U201-QB)
- U201 pad 2: Net-(U201-A) -> Net-(U201-QC)
- U201 pad 3: GND -> Net-(U201-QD)
- U201 pad 4: Net-(U201-Y) -> Net-(U201-QE)
- U201 pad 5: +3.3V -> Net-(U201-QF)
- U202 pad 2: Net-(U202-A) -> Net-(U201-QA)
- U203 pad 1: Net-(U203-QB) -> OE
- U203 pad 2: Net-(U203-QC) -> Net-(U201-QB)
- U203 pad 3: Net-(U203-QD) -> GND
- U203 pad 4: Net-(U203-QE) -> Net-(U203-Y)
- U203 pad 5: Net-(U203-QF) -> +3.3V
- U204 pad 2: Net-(U204-A) -> Net-(U201-QC)
- U205 pad 2: Net-(U205-A) -> Net-(U201-QD)
- U206 pad 1: Net-(U206-QB) -> OE
- U206 pad 2: unconnected-(U206-QC-Pad2) -> Net-(U201-QE)
- U206 pad 3: unconnected-(U206-QD-Pad3) -> GND
- U206 pad 4: unconnected-(U206-QE-Pad4) -> Net-(U206-Y)
- U206 pad 5: unconnected-(U206-QF-Pad5) -> +3.3V
- U207 pad 2: Net-(U207-A) -> Net-(U201-QF)
- U208 pad 2: Net-(U208-A) -> Net-(U201-QG)
- U209 pad 2: Net-(U209-A) -> Net-(U201-QH)
- U210 pad 1: OE -> Net-(U210-QB)
- U210 pad 2: Net-(U210-A) -> Net-(U210-QC)
- U210 pad 3: GND -> Net-(U210-QD)
- U210 pad 4: Net-(U210-Y) -> Net-(U210-QE)
- U210 pad 5: +3.3V -> Net-(U210-QF)
- U211 pad 1: Net-(U204-A) -> OE
- U211 pad 2: Net-(U207-A) -> Net-(U210-QA)
- U211 pad 3: Net-(U209-A) -> GND
- U211 pad 4: Net-(U211-QE) -> Net-(U211-Y)
- U211 pad 5: Net-(U211-QF) -> +3.3V
- U212 pad 1: Net-(U205-A) -> OE
- U212 pad 2: Net-(U208-A) -> Net-(U210-QB)
- U212 pad 3: Net-(U210-A) -> GND
- U212 pad 4: Net-(U212-QE) -> Net-(U212-Y)
- U212 pad 5: Net-(U212-QF) -> +3.3V
- U213 pad 2: Net-(U211-QE) -> Net-(U210-QC)
- U214 pad 2: Net-(U212-QE) -> Net-(U210-QD)
- U215 pad 2: Net-(U211-QF) -> Net-(U210-QE)
- U216 pad 2: Net-(U212-QF) -> Net-(U210-QF)
- U217 pad 2: Net-(U211-QG) -> Net-(U210-QG)
- U218 pad 2: Net-(U212-QG) -> Net-(U210-QH)
- U219 pad 1: OE -> Net-(U219-QB)
- U219 pad 2: Net-(U211-QH) -> Net-(U219-QC)
- U219 pad 3: GND -> Net-(U219-QD)
- U219 pad 4: Net-(U219-Y) -> Net-(U219-QE)
- U219 pad 5: +3.3V -> Net-(U219-QF)
- U220 pad 2: Net-(U212-QH) -> Net-(U219-QA)
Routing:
- net GND: track 0.00 -> 163.7 mm, vias 0 -> 95
- net CLK: track 0.00 -> 151.8 mm, vias 0 -> 8
- net OE: track 0.00 -> 148.2 mm, vias 0 -> 2
- net LATCH: track 0.00 -> 146.4 mm, vias 0 -> 6
- net ~{CLR}: track 0.00 -> 130.6 mm, vias 0 -> 5
- net Net-(U219-QH): track 0.00 -> 95.9 mm
- net DATA1: track 0.00 -> 87.4 mm, vias 0 -> 4
- net VBUS: track 0.00 -> 80.6 mm, vias 0 -> 21
- net +3.3V: track 0.00 -> 77.5 mm, vias 0 -> 43
- net +5V: track 0.00 -> 68.7 mm, vias 0 -> 4
- net Net-(U219-QB): track 0.00 -> 55.6 mm, vias 0 -> 2
- net Net-(U219-QA): track 0.00 -> 52.7 mm, vias 0 -> 2
- net I^{2}C_{SCL3V3}: track 0.00 -> 51.4 mm, vias 0 -> 2
- net Net-(U219-QH'): track 0.00 -> 51.2 mm, vias 0 -> 2
- net DATA2: track 0.00 -> 50.9 mm, vias 0 -> 2
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- added copper zone on F.Cu, net +3.3V
- added copper zone on In2.Cu, net +3.3V
- added copper zone on B.Cu, net GND
- added copper zone on F.Cu, net GND
- added copper zone on In1.Cu, net GND
- added copper zone on F.Cu, net Net-(Q105-S-Pad1)
- added copper zone on B.Cu, net Net-(U102-VCC)
- added copper zone on F.Cu, net Net-(U102-VCC)
- added copper zone on B.Cu, net VBUS
- added copper zone on F.Cu, net VBUS
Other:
- board size 90 x 85 mm -> 70 x 70.5 mm
- board text added: "GND"
- board text added: "NURDspace USB PD PPS 3.3-20V / 3A"
- board text added: "V_{OUT}"
- board text added: "_fun"
- board text added: "b00t"
- board text removed: "Tested:"

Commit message: Added new version of artifact generator
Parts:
- added D103: amber, LED_SMD:LED_0603_1608Metric, F.Cu at (103.0, 61.2)
- added R119: 180R, Resistor_SMD:R_0805_2012Metric, F.Cu at (132.0, 80.0)
- added R120: 5K1, Resistor_SMD:R_0805_2012Metric, F.Cu at (103.0, 55.5)
- J201: value BM05B -> BM06B; footprint 0_NRD_footprints:J_BM05B-GHS-TBT -> 0_NRD_footprints:J_BM06B-GHS-TBT
- moved J201 1.20 mm to (165.2, 63.9)
- moved C115 1.00 mm to (138.0, 80.0)
- moved R115 1.00 mm to (134.0, 80.0)
- moved R118 1.00 mm to (136.0, 80.0)
- moved D224 0.70 mm to (147.3, 62.3)
- moved D225 0.70 mm to (147.3, 64.9)
- moved D226 0.70 mm to (147.3, 67.5)
- moved D227 0.70 mm to (147.3, 70.1)
- moved D228 0.70 mm to (147.3, 72.7)
- moved D219 0.69 mm to (122.7, 62.3)
- moved D220 0.69 mm to (122.7, 64.9)
- moved D221 0.69 mm to (122.7, 67.5)
- moved D222 0.69 mm to (122.7, 70.1)
- moved D223 0.69 mm to (122.7, 72.7)
- moved D101 0.12 mm to (103.0, 59.4)
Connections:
- J201 pad 1: +3.3V -> VBUS
- J201 pad 2: Net-(J201-Pin_2) -> +3.3V
- J201 pad 3: CLK -> Net-(J201-Pin_3)
- J201 pad 4: LATCH -> CLK
- J201 pad 5: GND -> LATCH
- U102 pad 7: unconnected-(U102-NC-Pad7) -> Net-(U102-GPIO)
- U104 pad L1: Net-(U103-GPIO14/TOUCH14/ADC2_CH3/FSPIWP/FSPIDQS/SUBSPIWP) -> Net-(R119-Pad2)
- U222 pad 4: Net-(J201-Pin_2) -> Net-(J201-Pin_3)
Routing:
- net Net-(J201-Pin_3): track 0.00 -> 29.3 mm, vias 0 -> 2
- net Net-(J201-Pin_2): track 29.3 -> 0.00 mm, vias 2 -> 0
- net Net-(U103-GPIO14/TOUCH14/ADC2_CH3/FSPIWP/FSPIDQS/SUBSPIWP): track 14.8 -> 36.2 mm, vias 0 -> 4
- net Net-(R119-Pad2): track 0.00 -> 14.5 mm, vias 0 -> 1
- net Net-(U102-GPIO): track 0.00 -> 12.7 mm, vias 0 -> 2
- net Net-(U219-QH): track 95.9 -> 84.6 mm, vias 0 -> 2
- net Net-(D103-A): track 0.00 -> 11.3 mm
- net Net-(D102-A): track 7.04 -> 8.71 mm
- net VBUS: track 80.6 -> 82.3 mm, vias 21 -> 22
- net I^{2}C_{SCL5V}: track 32.6 -> 33.6 mm
- net I^{2}C_{SDA5V}: track 39.8 -> 40.6 mm
- net CLK: track 151.8 -> 151.0 mm
- net Net-(D228-A): track 14.3 -> 15.0 mm
- net Net-(D227-A): track 11.9 -> 12.6 mm
- net Net-(D226-A): track 10.5 -> 11.2 mm
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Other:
- outline, holes or cut-outs redrawn
- board text added: "10"
- board text added: "11"
- board text added: "12"
- board text added: "13"
- board text added: "14"
- board text added: "15"
- board text added: "16"
- board text added: "17"
- board text added: "18"
- board text added: "19"
- board text added: "20"
- board text added: "3"
- board text added: "4"
- board text added: "5"
- board text added: "6"
- board text added: "7"
- board text added: "8"
- board text added: "9"
- board text added: "MCU status"
- board text added: "PD V_{OUT}"
- board text added: "PD status"
- board text added: "V_{OUT} 3V3 DATA CLK LATCH GND"
